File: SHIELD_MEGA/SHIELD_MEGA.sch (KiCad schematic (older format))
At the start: 1 part

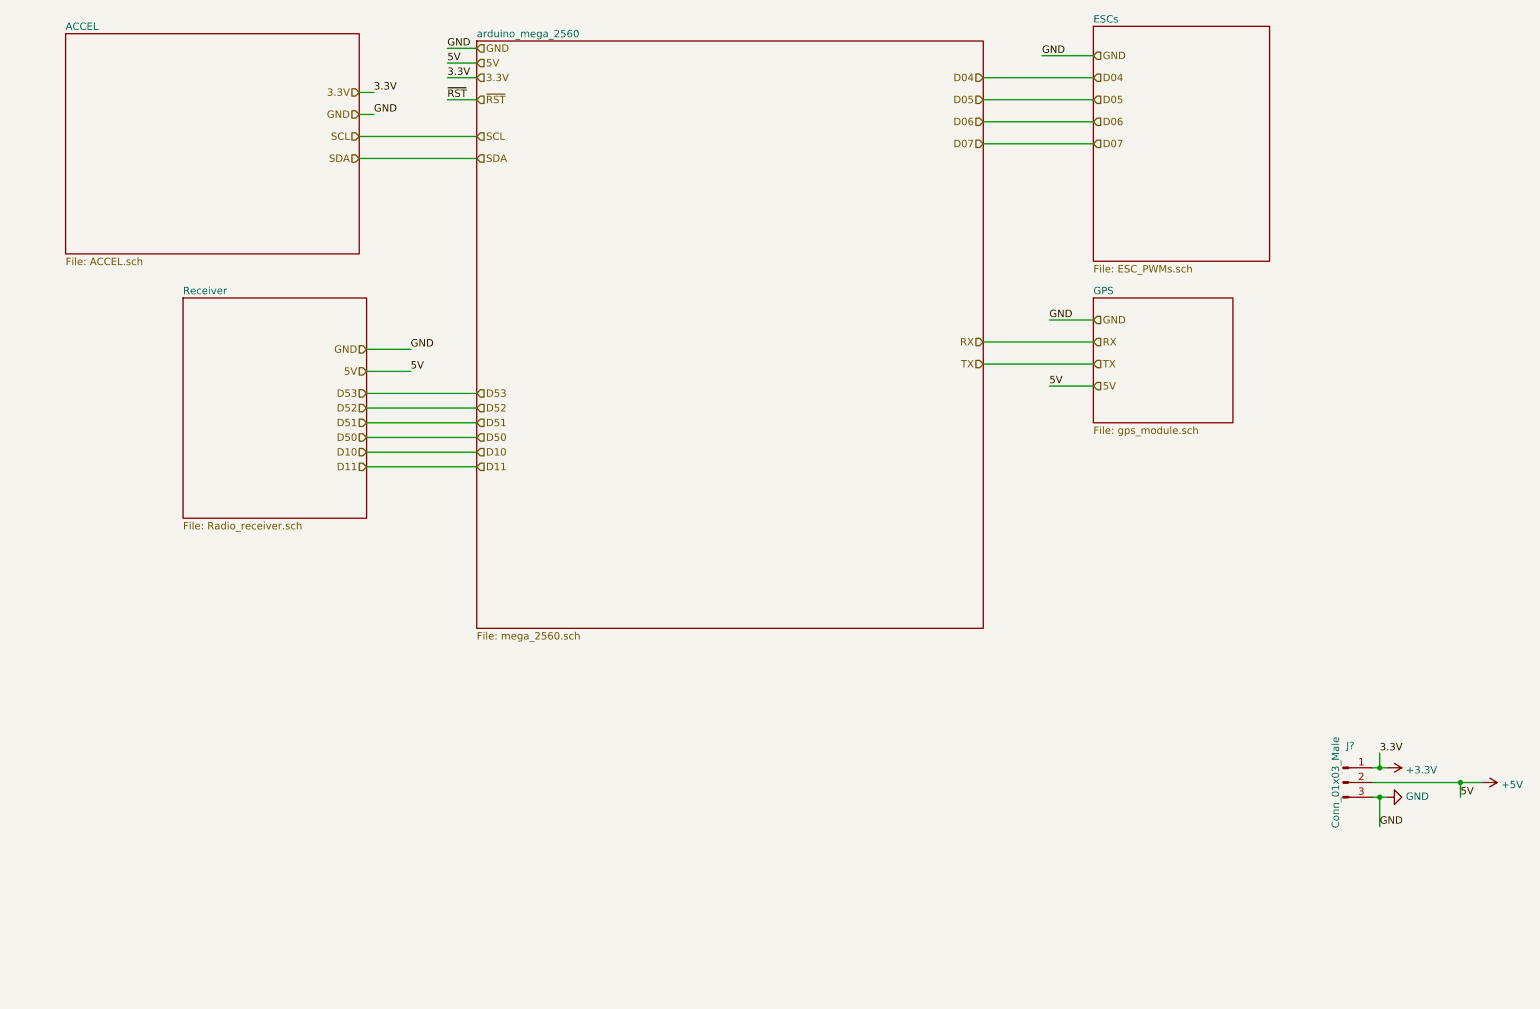
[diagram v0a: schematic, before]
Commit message: fixing labels type
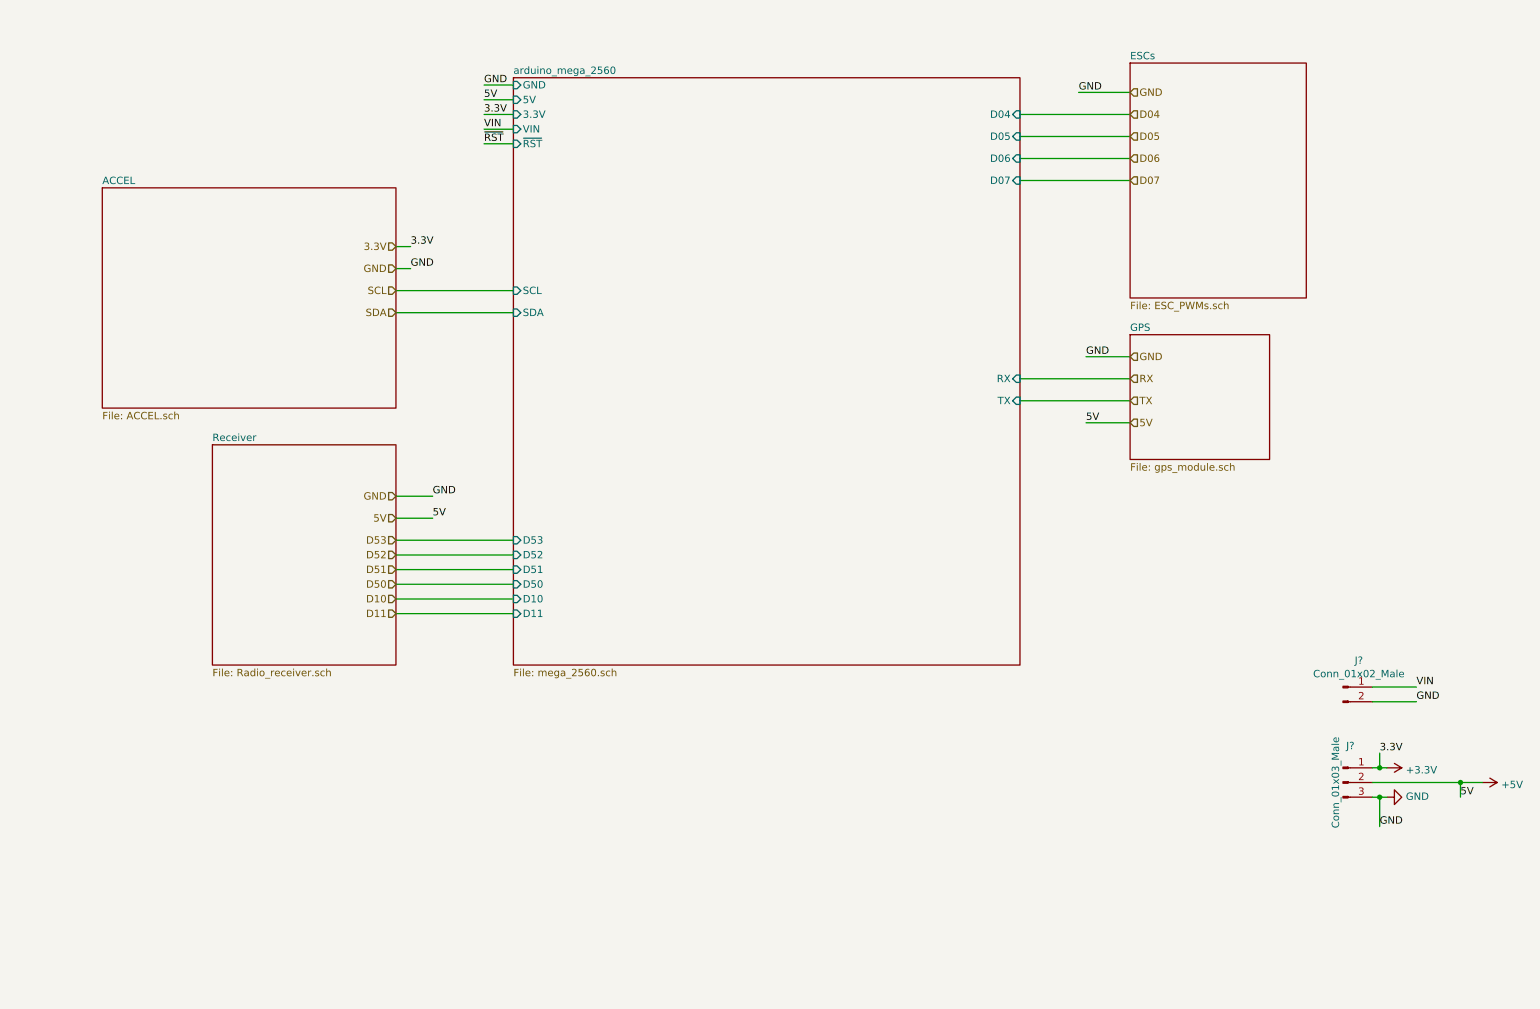
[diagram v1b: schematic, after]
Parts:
- added J?: Conn_01x02_Male, symbol Connector:Conn_01x02_Male
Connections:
- net GND: now also J?.2 (Pin_2)
- new net VIN: J?.1 (Pin_1)
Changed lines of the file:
@@
 $Descr A4 11693 8268
 encoding utf-8
-Sheet 1 7
+Sheet 1 9
 Title ""
 Date ""
@@
 Comment4 ""
 $EndDescr
-$Sheet
-S 3850 900  3450 4000
-U 6194FDB3
-F0 "arduino_mega_2560" 50
-F1 "mega_2560.sch" 50
-$EndSheet
 $Comp
 L Connector:Conn_01x03_Male J?
@@
 Wire Wire Line
 	9950 6050 10000 6050
-Text HLabel 3850 950  2    50   Input ~ 0
-GND
-Text Label 3650 950  0    50   ~ 0
-GND
-Wire Wire Line
-	3650 950  3850 950
+Text Label 3900 1200 0    50   ~ 0
+GND
+Wire Wire Line
+	3900 1200 4100 1200
 Wire Wire Line
 	10000 6250 10000 6050
@@
 Wire Wire Line
 	10000 5850 10050 5850
-Text HLabel 3850 1150 2    50   Input ~ 0
-3.3V
-Text HLabel 3850 1050 2    50   Input ~ 0
-5V
-Wire Wire Line
-	3850 1050 3650 1050
-Wire Wire Line
-	3850 1150 3650 1150
-Text Label 3650 1050 0    50   ~ 0
-5V
-Text Label 3650 1150 0    50   ~ 0
-3.3V
-Text HLabel 3850 1300 2    50   Input ~ 0
+Wire Wire Line
+	4100 1300 3900 1300
+Wire Wire Line
+	4100 1400 3900 1400
+Text Label 3900 1300 0    50   ~ 0
+5V
+Text Label 3900 1400 0    50   ~ 0
+3.3V
+Text Label 3900 1600 0    50   ~ 0
 ~RST
-Text Label 3650 1300 0    50   ~ 0
-~RST
-Wire Wire Line
-	3650 1300 3850 1300
-$Sheet
-S 1050 850  2000 1500
+$Sheet
+S 1300 1900 2000 1500
 U 619602F2
 F0 "ACCEL" 50
 F1 "ACCEL.sch" 50
 $EndSheet
-Text HLabel 3050 1250 0    50   Input ~ 0
-3.3V
-Text HLabel 3050 1400 0    50   Input ~ 0
-GND
-Text HLabel 3050 1550 0    50   Input ~ 0
+Text HLabel 3300 2300 0    50   Input ~ 0
+3.3V
+Text HLabel 3300 2450 0    50   Input ~ 0
+GND
+Text HLabel 3300 2600 0    50   Input ~ 0
 SCL
-Text HLabel 3050 1700 0    50   Input ~ 0
+Text HLabel 3300 2750 0    50   Input ~ 0
 SDA
 Wire Wire Line
-	3050 1250 3150 1250
-Text Label 3150 1250 0    50   ~ 0
-3.3V
-Text Label 3150 1400 0    50   ~ 0
-GND
-Wire Wire Line
-	3150 1400 3050 1400
-Text HLabel 3850 1550 2    50   Input ~ 0
-SCL
-Text HLabel 3850 1700 2    50   Input ~ 0
-SDA
-Text HLabel 8050 1000 2    50   Input ~ 0
-GND
-$Sheet
-S 8050 800  1200 1600
+	3300 2300 3400 2300
+Text Label 3400 2300 0    50   ~ 0
+3.3V
+Text Label 3400 2450 0    50   ~ 0
+GND
+Wire Wire Line
+	3400 2450 3300 2450
+Text HLabel 8300 1250 2    50   Input ~ 0
+GND
+$Sheet
+S 8300 1050 1200 1600
 U 619656BE
 F0 "ESCs" 50
 F1 "ESC_PWMs.sch" 50
 $EndSheet
-Text HLabel 8050 1150 2    50   Input ~ 0
+Text HLabel 8300 1400 2    50   Input ~ 0
 D04
-Text HLabel 8050 1300 2    50   Input ~ 0
+Text HLabel 8300 1550 2    50   Input ~ 0
 D05
-Text HLabel 8050 1450 2    50   Input ~ 0
+Text HLabel 8300 1700 2    50   Input ~ 0
 D06
-Text HLabel 8050 1600 2    50   Input ~ 0
+Text HLabel 8300 1850 2    50   Input ~ 0
 D07
 Wire Wire Line
-	3050 1550 3850 1550
-Wire Wire Line
-	3850 1700 3050 1700
-Text Label 7700 1000 0    50   ~ 0
-GND
-Wire Wire Line
-	7700 1000 8050 1000
-Text HLabel 7300 1150 0    50   Input ~ 0
-D04
-Text HLabel 7300 1300 0    50   Input ~ 0
-D05
-Text HLabel 7300 1450 0    50   Input ~ 0
-D06
-Text HLabel 7300 1600 0    50   Input ~ 0
-D07
-Wire Wire Line
-	7300 1600 8050 1600
-Wire Wire Line
-	8050 1450 7300 1450
-Wire Wire Line
-	7300 1300 8050 1300
-Wire Wire Line
-	8050 1150 7300 1150
-$Sheet
-S 1850 2650 1250 1500
+	3300 2600 4100 2600
+Wire Wire Line
+	4100 2750 3300 2750
+Text Label 7950 1250 0    50   ~ 0
+GND
+Wire Wire Line
+	7950 1250 8300 1250
+Wire Wire Line
+	7550 1850 8300 1850
+Wire Wire Line
+	8300 1700 7550 1700
+Wire Wire Line
+	7550 1550 8300 1550
+Wire Wire Line
+	8300 1400 7550 1400
+$Sheet
+S 2050 3650 1250 1500
 U 6197A5F1
 F0 "Receiver" 50
@@
 $EndSheet
 $Sheet
-S 8050 2650 950  850
+S 8300 2900 950  850
 U 6197A819
 F0 "GPS" 50
 F1 "gps_module.sch" 50
 $EndSheet
-Text HLabel 8050 2800 2    50   Input ~ 0
-GND
-Text Label 7750 2800 0    50   ~ 0
-GND
-Wire Wire Line
-	7750 2800 8050 2800
-Text HLabel 8050 3250 2    50   Input ~ 0
-5V
-Text HLabel 8050 2950 2    50   Input ~ 0
+Text HLabel 8300 3050 2    50   Input ~ 0
+GND
+Text Label 8000 3050 0    50   ~ 0
+GND
+Wire Wire Line
+	8000 3050 8300 3050
+Text HLabel 8300 3500 2    50   Input ~ 0
+5V
+Text HLabel 8300 3200 2    50   Input ~ 0
 RX
-Text HLabel 8050 3100 2    50   Input ~ 0
+Text HLabel 8300 3350 2    50   Input ~ 0
 TX
-Text Label 7750 3250 0    50   ~ 0
-5V
-Wire Wire Line
-	7750 3250 8050 3250
-Text HLabel 7300 2950 0    50   Input ~ 0
-RX
-Text HLabel 7300 3100 0    50   Input ~ 0
-TX
-Wire Wire Line
-	7300 2950 8050 2950
-Wire Wire Line
-	7300 3100 8050 3100
-Text HLabel 3100 3000 0    50   Input ~ 0
-GND
-Text HLabel 3100 3150 0    50   Input ~ 0
-5V
-Text Label 3400 3000 0    50   ~ 0
-GND
-Wire Wire Line
-	3400 3000 3100 3000
-Wire Wire Line
-	3100 3150 3400 3150
-Text Label 3400 3150 0    50   ~ 0
-5V
-Text HLabel 3100 3300 0    50   Input ~ 0
+Text Label 8000 3500 0    50   ~ 0
+5V
+Wire Wire Line
+	8000 3500 8300 3500
+Wire Wire Line
+	7550 3200 8300 3200
+Wire Wire Line
+	7550 3350 8300 3350
+Text HLabel 3300 4000 0    50   Input ~ 0
+GND
+Text HLabel 3300 4150 0    50   Input ~ 0
+5V
+Text Label 3550 4000 0    50   ~ 0
+GND
+Wire Wire Line
+	3550 4000 3300 4000
+Wire Wire Line
+	3300 4150 3550 4150
+Text Label 3550 4150 0    50   ~ 0
+5V
+Text HLabel 3300 4300 0    50   Input ~ 0
 D53
-Text HLabel 3100 3400 0    50   Input ~ 0
+Text HLabel 3300 4400 0    50   Input ~ 0
 D52
-Text HLabel 3100 3500 0    50   Input ~ 0
+Text HLabel 3300 4500 0    50   Input ~ 0
 D51
-Text HLabel 3100 3600 0    50   Input ~ 0
+Text HLabel 3300 4600 0    50   Input ~ 0
 D50
-Text HLabel 3100 3800 0    50   Input ~ 0
+Text HLabel 3300 4800 0    50   Input ~ 0
 D11
-Text HLabel 3100 3700 0    50   Input ~ 0
+Text HLabel 3300 4700 0    50   Input ~ 0
 D10
-Text HLabel 3850 3300 2    50   Input ~ 0
-D53
-Text HLabel 3850 3400 2    50   Input ~ 0
-D52
-Text HLabel 3850 3500 2    50   Input ~ 0
-D51
-Text HLabel 3850 3600 2    50   Input ~ 0
-D50
-Text HLabel 3850 3700 2    50   Input ~ 0
-D10
-Text HLabel 3850 3800 2    50   Input ~ 0
-D11
-Wire Wire Line
-	3100 3300 3850 3300
-Wire Wire Line
-	3850 3400 3100 3400
-Wire Wire Line
-	3100 3500 3850 3500
-Wire Wire Line
-	3850 3600 3100 3600
-Wire Wire Line
-	3100 3700 3850 3700
-Wire Wire Line
-	3850 3800 3100 3800
+Wire Wire Line
+	3300 4300 4100 4300
+Wire Wire Line
+	4100 4400 3300 4400
+Wire Wire Line
+	3300 4500 4100 4500
+Wire Wire Line
+	4100 4600 3300 4600
+Wire Wire Line
+	3300 4700 4100 4700
+Wire Wire Line
+	4100 4800 3300 4800
+Wire Wire Line
+	3900 1600 4100 1600
+Wire Wire Line
+	4100 1500 3900 1500
+Text Label 3900 1500 0    50   ~ 0
+VIN
+$Comp
+L Connector:Conn_01x02_Male J?
+U 1 1 61A80B16
+P 9750 5300
+F 0 "J?" H 9858 5481 50  0000 C CNN
+F 1 "Conn_01x02_Male" H 9858 5390 50  0000 C CNN
+F 2 "" H 9750 5300 50  0001 C CNN
+F 3 "~" H 9750 5300 50  0001 C CNN
+	1    9750 5300
+	1    0    0    -1
+$EndComp
+Text Label 10250 5300 0    50   ~ 0
+VIN
+Wire Wire Line
+	10250 5300 9950 5300
+Wire Wire Line
+	9950 5400 10250 5400
+Text Label 10250 5400 0    50   ~ 0
+GND
+$Sheet
+S 4100 1150 3450 4000
+U 6194FDB3
+F0 "arduino_mega_2560" 50
+F1 "mega_2560.sch" 50
+F2 "GND" I L 4100 1200 50
+F3 "5V" I L 4100 1300 50
+F4 "3.3V" I L 4100 1400 50
+F5 "VIN" I L 4100 1500 50
+F6 "~RST" I L 4100 1600 50
+F7 "SCL" I L 4100 2600 50
+F8 "SDA" I L 4100 2750 50
+F9 "D53" I L 4100 4300 50
+F10 "D52" I L 4100 4400 50
+F11 "D51" I L 4100 4500 50
+F12 "D50" I L 4100 4600 50
+F13 "D10" I L 4100 4700 50
+F14 "D11" I L 4100 4800 50
+F15 "D04" I R 7550 1400 50
+F16 "D05" I R 7550 1550 50
+F17 "D06" I R 7550 1700 50
+F18 "D07" I R 7550 1850 50
+F19 "RX" I R 7550 3200 50
+F20 "TX" I R 7550 3350 50
+$EndSheet
 $EndSCHEMATC

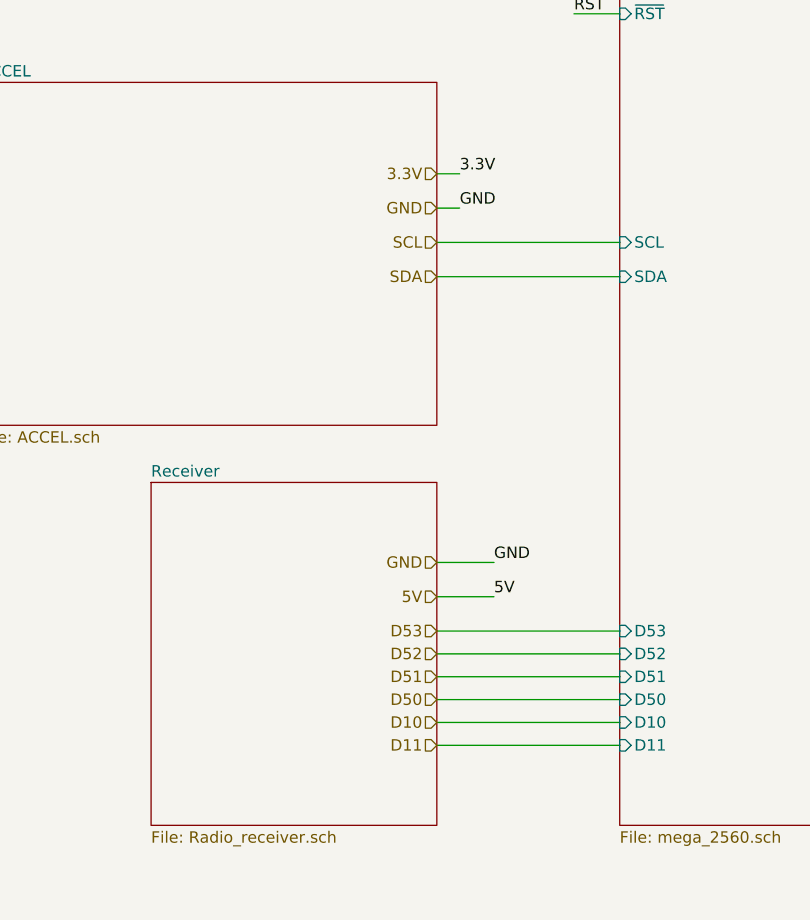
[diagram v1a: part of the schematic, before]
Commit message: updating labels type
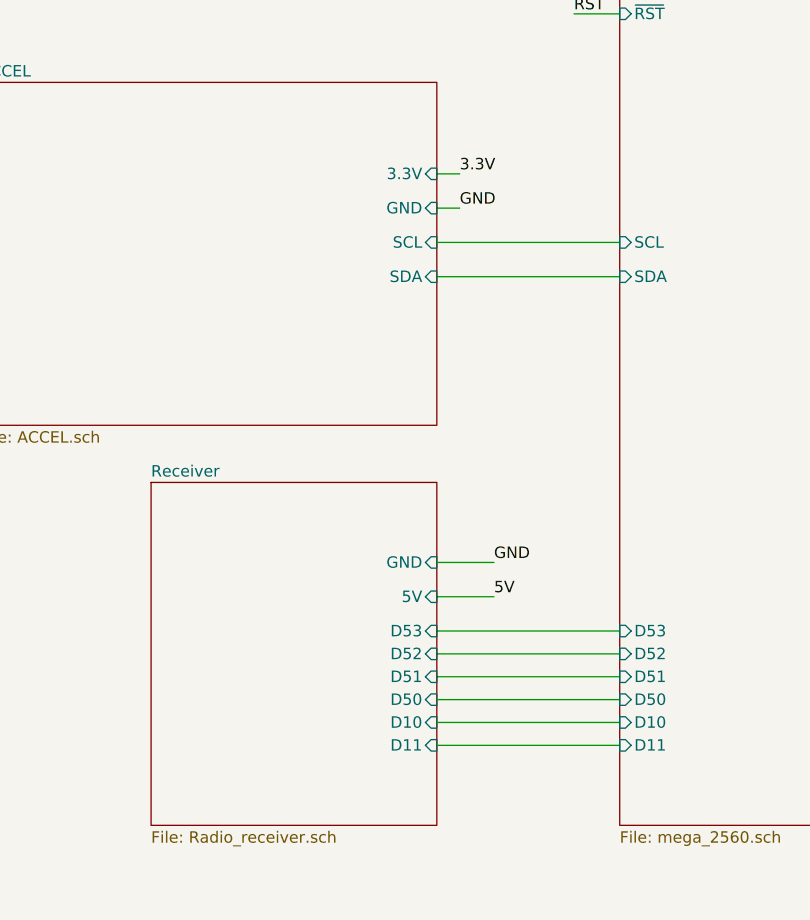
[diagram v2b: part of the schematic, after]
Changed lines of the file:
@@
 F0 "ACCEL" 50
 F1 "ACCEL.sch" 50
+F2 "3.3V" I R 3300 2300 50
+F3 "GND" I R 3300 2450 50
+F4 "SCL" I R 3300 2600 50
+F5 "SDA" I R 3300 2750 50
 $EndSheet
-Text HLabel 3300 2300 0    50   Input ~ 0
-3.3V
-Text HLabel 3300 2450 0    50   Input ~ 0
-GND
-Text HLabel 3300 2600 0    50   Input ~ 0
-SCL
-Text HLabel 3300 2750 0    50   Input ~ 0
-SDA
 Wire Wire Line
 	3300 2300 3400 2300
@@
 	8300 1400 7550 1400
 $Sheet
-S 2050 3650 1250 1500
-U 6197A5F1
-F0 "Receiver" 50
-F1 "Radio_receiver.sch" 50
-$EndSheet
-$Sheet
 S 8300 2900 950  850
 U 6197A819
@@
 Wire Wire Line
 	7550 3350 8300 3350
-Text HLabel 3300 4000 0    50   Input ~ 0
-GND
-Text HLabel 3300 4150 0    50   Input ~ 0
-5V
 Text Label 3550 4000 0    50   ~ 0
 GND
@@
 Text Label 3550 4150 0    50   ~ 0
 5V
-Text HLabel 3300 4300 0    50   Input ~ 0
-D53
-Text HLabel 3300 4400 0    50   Input ~ 0
-D52
-Text HLabel 3300 4500 0    50   Input ~ 0
-D51
-Text HLabel 3300 4600 0    50   Input ~ 0
-D50
-Text HLabel 3300 4800 0    50   Input ~ 0
-D11
-Text HLabel 3300 4700 0    50   Input ~ 0
-D10
 Wire Wire Line
 	3300 4300 4100 4300
@@
 F20 "TX" I R 7550 3350 50
 $EndSheet
+$Sheet
+S 2050 3650 1250 1500
+U 6197A5F1
+F0 "Receiver" 50
+F1 "Radio_receiver.sch" 50
+F2 "GND" I R 3300 4000 50
+F3 "5V" I R 3300 4150 50
+F4 "D53" I R 3300 4300 50
+F5 "D52" I R 3300 4400 50
+F6 "D51" I R 3300 4500 50
+F7 "D50" I R 3300 4600 50
+F8 "D10" I R 3300 4700 50
+F9 "D11" I R 3300 4800 50
+$EndSheet
 $EndSCHEMATC
